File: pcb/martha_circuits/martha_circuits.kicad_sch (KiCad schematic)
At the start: 11 parts, among them J1 Conn_01x06, J2 Conn_01x06, J3 Conn_01x06, J4 Conn_01x06, J5 IMU, U5 LM339

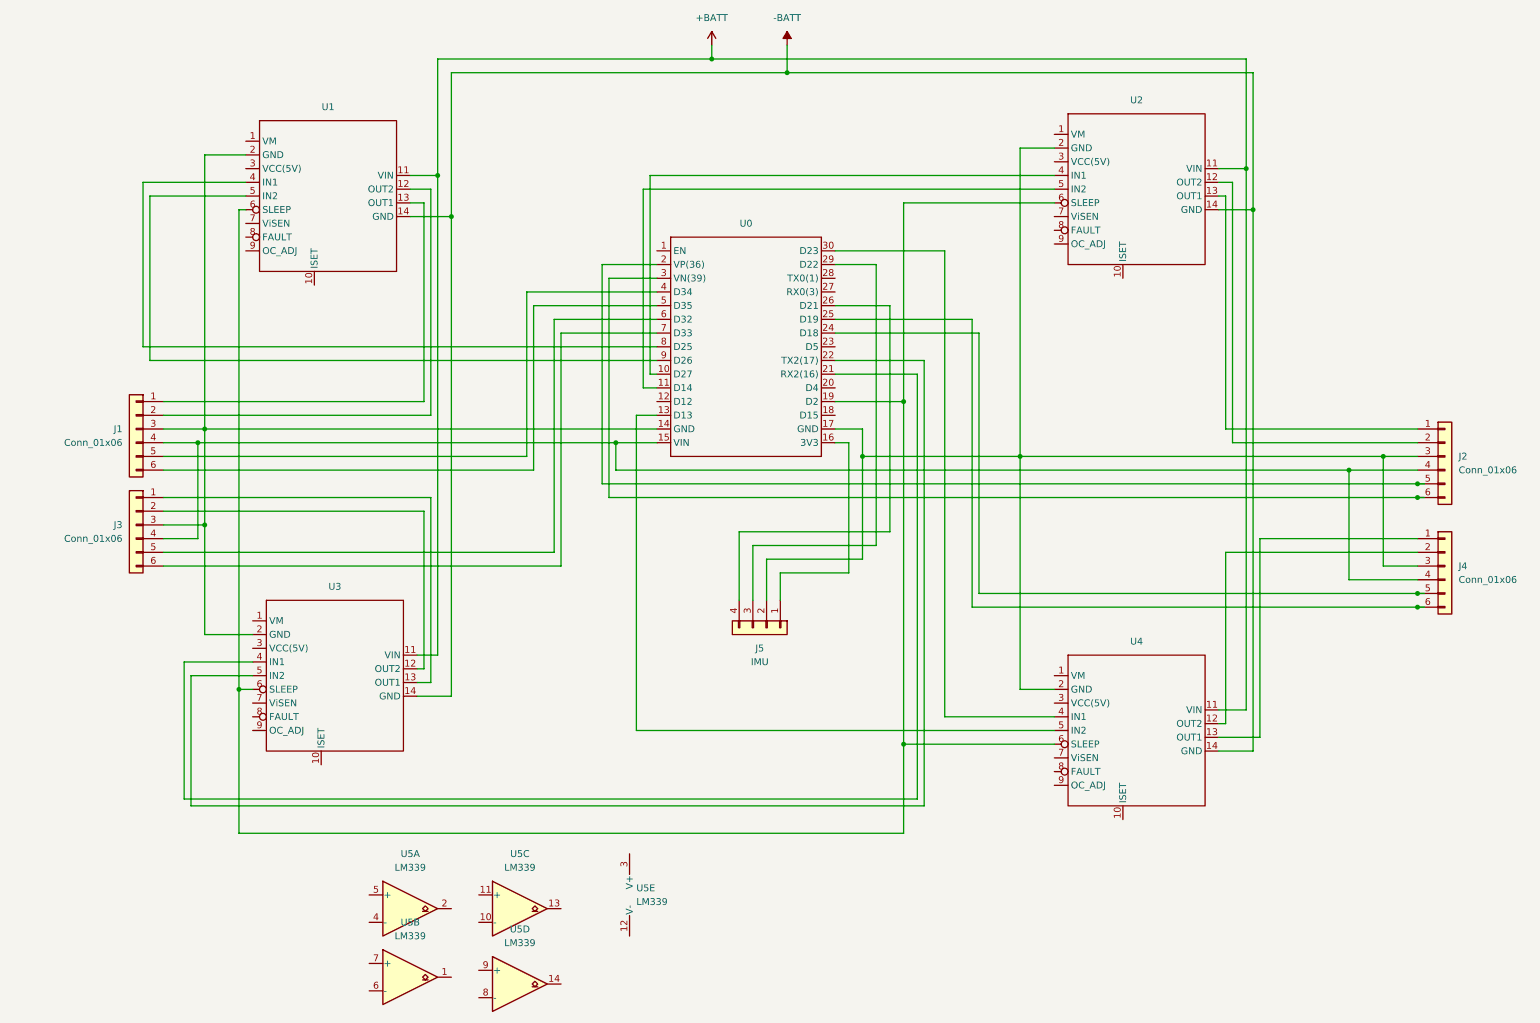
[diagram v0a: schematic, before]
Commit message: Component rearrangement, and use of power symbols to reduce wiring in schematic. Add Deans connector footprint
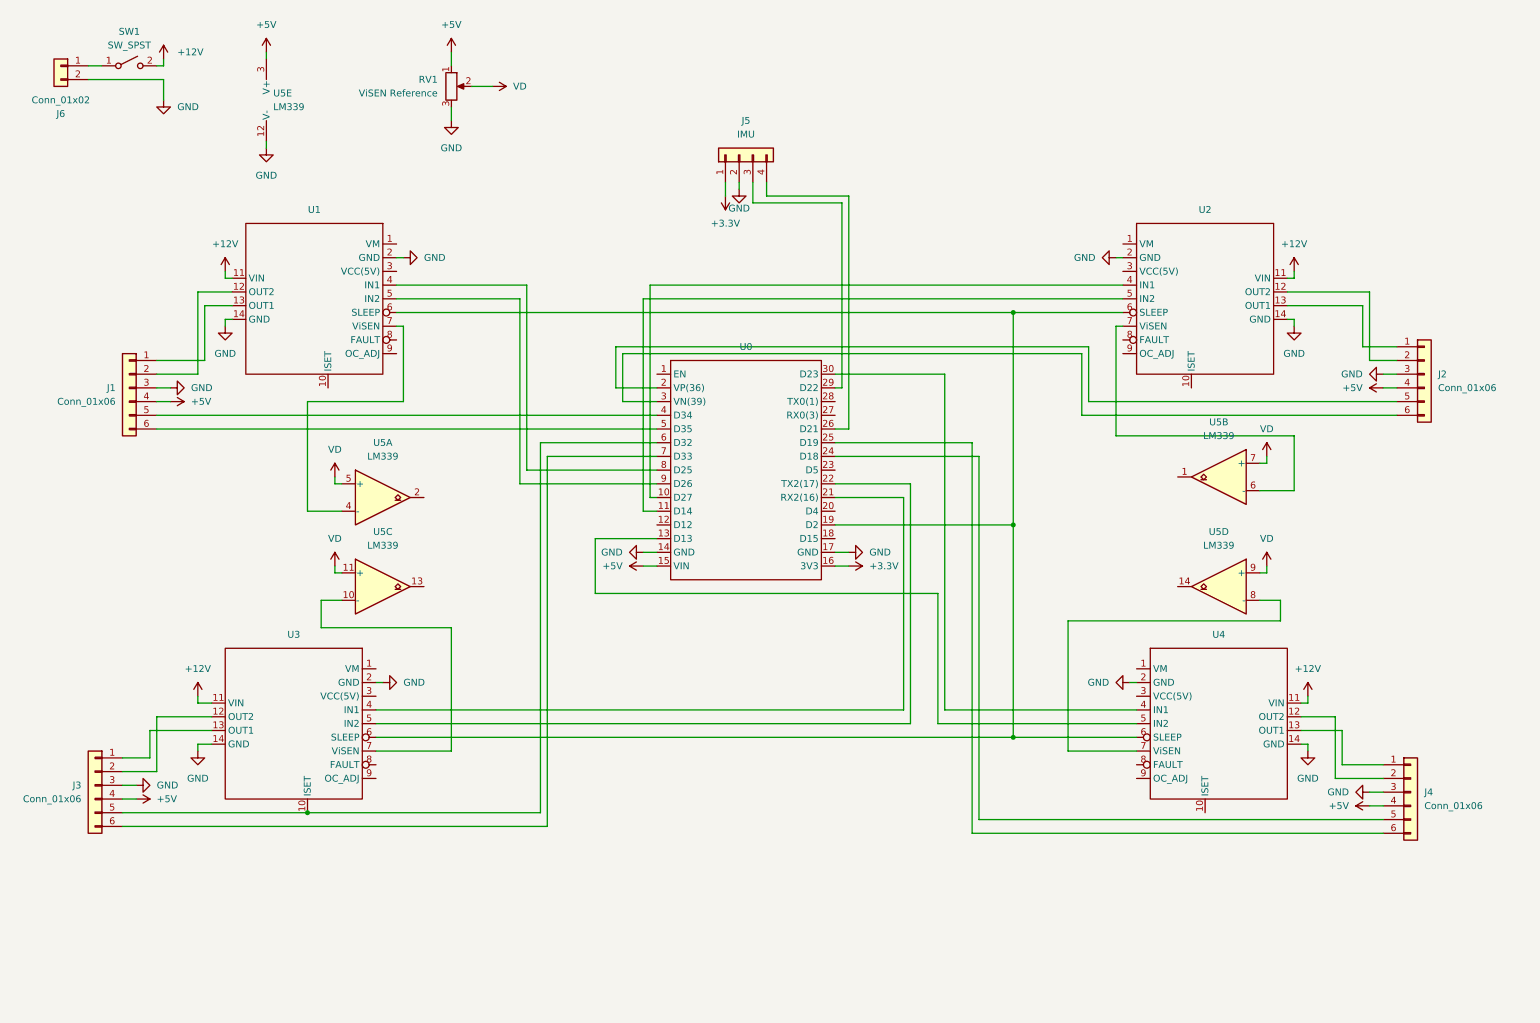
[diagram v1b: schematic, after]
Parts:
- added J6: Conn_01x02, My_Components:DEANS, symbol Connector_Generic:Conn_01x02
- added RV1: ViSEN Reference, symbol Device:R_Potentiometer
- added SW1: SW_SPST, symbol Switch:SW_SPST
- J1, J2, J3, J4: footprint Connector_PinHeader_1.00mm:PinHeader_1x06_P1.00mm_Horizontal -> Connector_PinHeader_2.54mm:PinHeader_1x06_P2.54mm_Horizontal
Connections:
- net -BATT is gone; now on net GND: U1.14 (GND), U2.14 (GND), U3.14 (GND), U4.14 (GND)
- net GND: now reaches J2.3 (Pin_3), J4.3 (Pin_3), J5.2 (Pin_2), U0.17 (GND), U2.2 (GND), U4.2 (GND)
- net GND: now also J1.3 (Pin_3), J3.3 (Pin_3), U0.14 (GND), U1.2 (GND), U3.2 (GND), U5.12 (V-), J6.2 (Pin_2), RV1.3
- net +5V: now reaches J1.4 (Pin_4), J2.4 (Pin_4), J3.4 (Pin_4), J4.4 (Pin_4), U0.15 (VIN)
- net +5V: now also U5.3 (V+), RV1.1
- net at J3.5 (Pin_5), U0.6 (D32): now also U3.10 (ISET)
- net at U5.10 (-): now also U3.7 (ViSEN)
- net VD: now reaches U5.11 (+)
- net VD: now also U5.5 (+), U5.7 (+), U5.9 (+), RV1.2
- net +3.3V: now reaches J5.1 (Pin_1), U0.16 (3V3)
- net at U1.7 (ViSEN): now also U5.4 (-)
- net at U4.7 (ViSEN): now also U5.8 (-)
- net at U2.7 (ViSEN): now also U5.6 (-)
- net +BATT renamed +12V
- net +12V: now also SW1.2 (B)
- new net: J6.1 (Pin_1), SW1.1 (A)
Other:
- company: (none) -> Niko and Juli @ USTA
- title: (none) -> Martha Circuit
- moved on the sheet: J1, J2, J3, J4, J5, U0, U1, U2, U3, U4
